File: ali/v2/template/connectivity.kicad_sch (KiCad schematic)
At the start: 27 parts, among them J7 Conn_01x03, J8 Vertical Ethernet, U3 TJA1462ATK, U4 LAN8742AI, Y2 25 MHz

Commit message: Globally remove LCSC labels, update MPNs and IOCs, add +5V monitoring to DAQs, fix some footprints
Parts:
- C24: MPN GRM21A5C2J471FWA1 -> GRM1885C1H471JA01
- C26: MPN GRM21AR72A224KAC5 -> GRM188R71H224KAC4
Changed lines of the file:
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@@
 			)
 		)
-		(property "MPN" "GRM21AR72A224KAC5"
+		(property "MPN" "GRM188R71H224KAC4"
 			(at 157.48 132.08 0)
 			(hide yes)
@@
 			)
 		)
-		(property "MPN" "GRM21A5C2J471FWA1"
+		(property "MPN" "GRM1885C1H471JA01"
 			(at 100.33 50.8 0)
 			(hide yes)

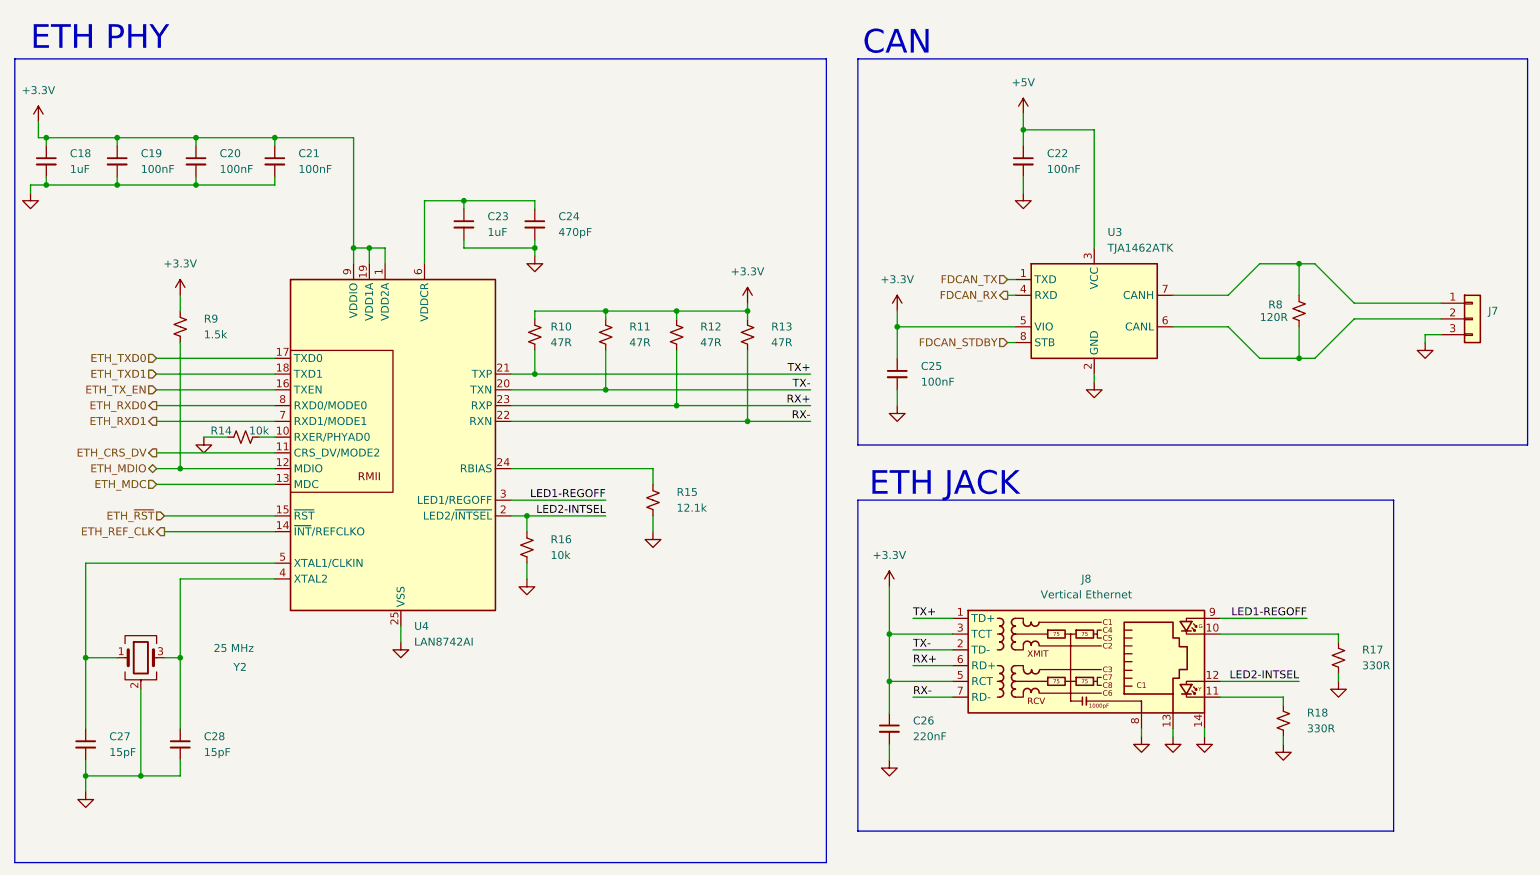
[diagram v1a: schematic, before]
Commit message: the great flatpak and kicad 10.0.6 migration
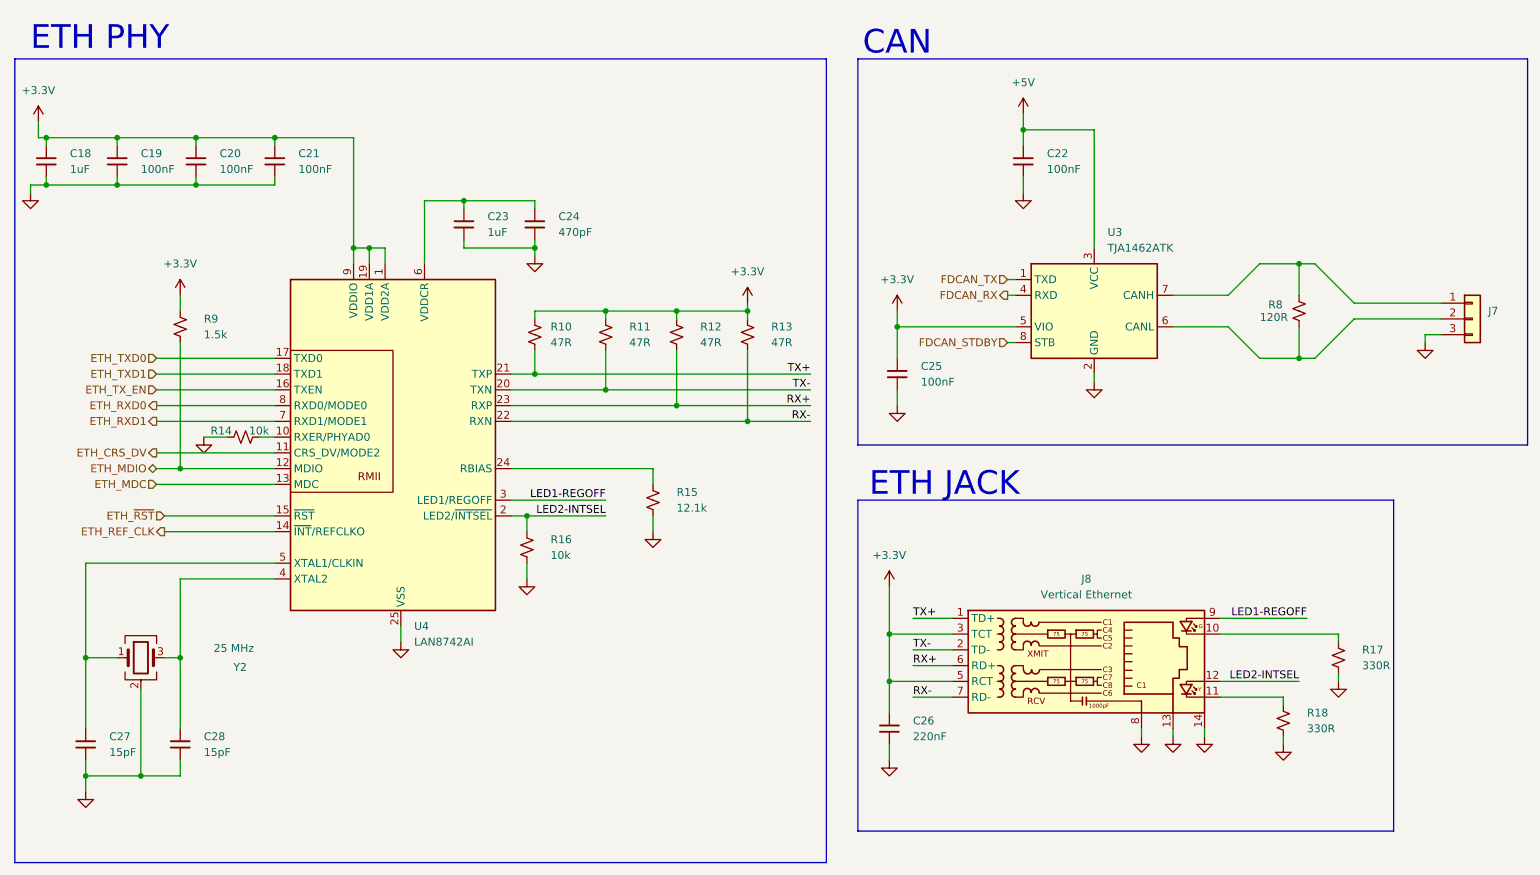
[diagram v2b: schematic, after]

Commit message: Fix 50R/60R widths
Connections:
- net CAN+: now reaches J7.1 (Pin_1), R8.2, U3.7 (CANH)
- net CAN-: now reaches J7.2 (Pin_2), R8.1, U3.6 (CANL)
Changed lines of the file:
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@@
+		)
+	)
+	(label "CAN-"
+		(at 205.7332 67.31 0)
+		(effects
+			(font
+				(size 1.27 1.27)
+			)
+			(justify left bottom)
+		)
+	)
+	(label "CAN+"
+		(at 205.74 62.23 0)
+		(effects
+			(font
+				(size 1.27 1.27)
+			)
+			(justify left bottom)
 		)
 	)
